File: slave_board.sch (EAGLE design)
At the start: 150 parts, among them IC3 ATMEGA2560-16AU, J11 1935161, J17 RJ45, J22 RJ45, J3 1935161, J6 1935161, K1 ORWH-SH-112D1F, Q1 PHB45NQ15T, Q2 PHB45NQ15T, Q3 BSS138L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

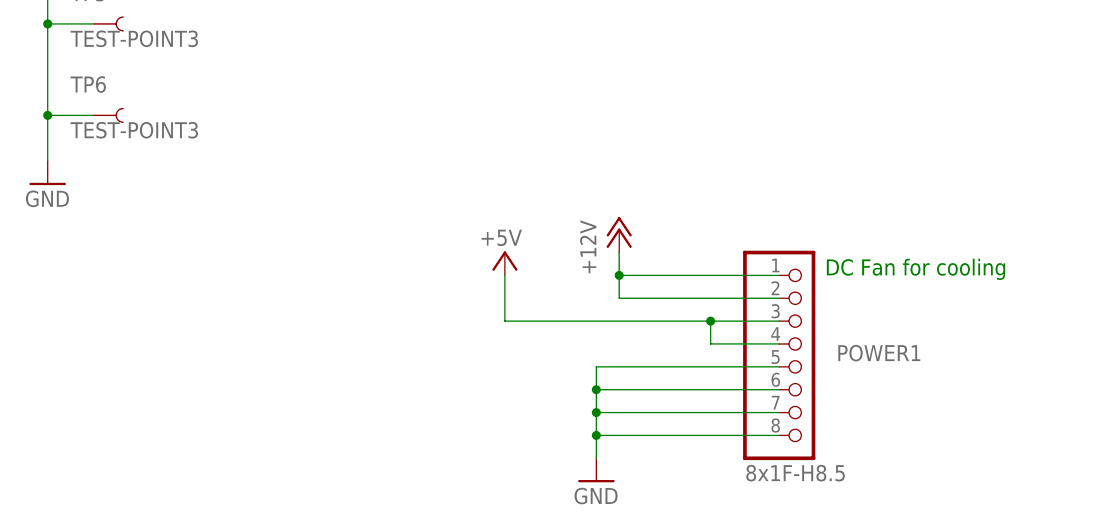
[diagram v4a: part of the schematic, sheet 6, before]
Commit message: More screw terminals
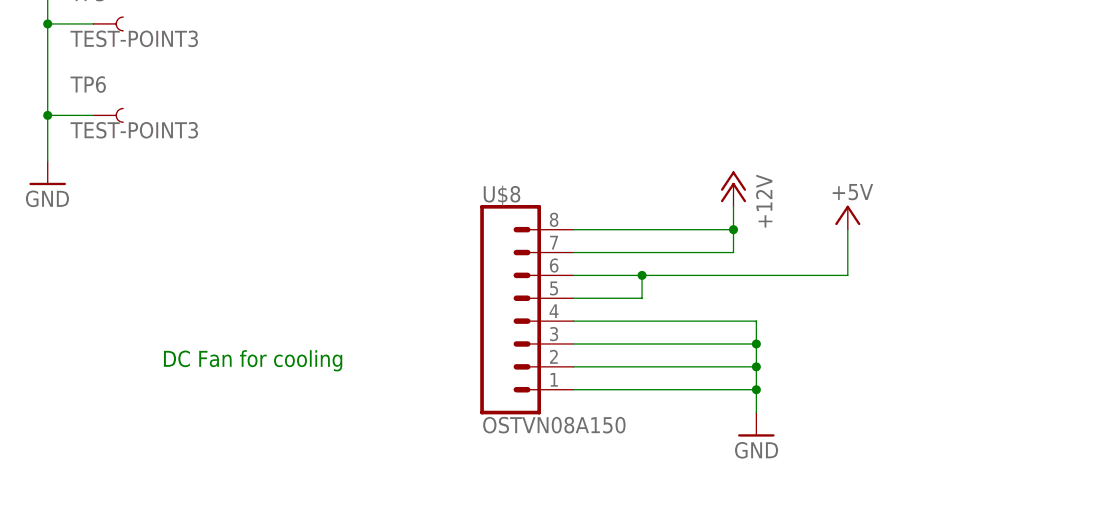
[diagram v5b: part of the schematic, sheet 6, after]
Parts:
- removed POWER1: 8x1F-H8.5, SmartPrj:PINHD-1X8
- added U$8: OSTVN08A150, smoothio:OSTVN08A150
- J18, J8: value (none) -> OSTVN08A150; device SparkFun-Connectors:CONN_08" -> smoothio:OSTVN08A150
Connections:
- net +12V: now also U$8.7, U$8.8; no longer POWER1.1, POWER1.2
- net +5V: now also U$8.5, U$8.6; no longer POWER1.3, POWER1.4
- net GND: now also U$8.1, U$8.2, U$8.3, U$8.4; no longer POWER1.5, POWER1.6, POWER1.7, POWER1.8
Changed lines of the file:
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@@
 <part name="GND83" library="supply1" library_urn="urn:adsk.eagle:library:371" deviceset="GND" device=""/>
 <part name="P+14" library="supply1" library_urn="urn:adsk.eagle:library:371" deviceset="+5V" device=""/>
-<part name="POWER1" library="SmartPrj" deviceset="PINHD-1X8" device="" value="8x1F-H8.5"/>
 <part name="P+37" library="supply1" library_urn="urn:adsk.eagle:library:371" deviceset="+12V" device=""/>
 <part name="P+4" library="supply1" library_urn="urn:adsk.eagle:library:371" deviceset="+5V" device=""/>
@@
 <part name="P+42" library="supply1" library_urn="urn:adsk.eagle:library:371" deviceset="+5V" device=""/>
 <part name="C24" library="rcl" library_urn="urn:adsk.eagle:library:334" deviceset="C-US" device="C0603" package3d_urn="urn:adsk.eagle:package:23616/2" value="0.1uF"/>
-<part name="J8" library="SparkFun-Connectors" library_urn="urn:adsk.eagle:library:513" deviceset="CONN_08" device="&quot;" package3d_urn="urn:adsk.eagle:package:38138/1"/>
-<part name="J18" library="SparkFun-Connectors" library_urn="urn:adsk.eagle:library:513" deviceset="CONN_08" device="&quot;" package3d_urn="urn:adsk.eagle:package:38138/1"/>
+<part name="J8" library="smoothio" deviceset="OSTVN08A150" device=""/>
+<part name="J18" library="smoothio" deviceset="OSTVN08A150" device=""/>
 <part name="JP14" library="SparkFun-Jumpers" library_urn="urn:adsk.eagle:library:528" deviceset="JUMPER-SMT_2_NC_TRACE" device="_NO-SILK" package3d_urn="urn:adsk.eagle:package:39286/1"/>
 <part name="J7" library="SparkFun-Connectors" library_urn="urn:adsk.eagle:library:513" deviceset="CONN_02" device="" package3d_urn="urn:adsk.eagle:package:38039/1"/>
@@
 <part name="GND63" library="supply1" library_urn="urn:adsk.eagle:library:371" deviceset="GND" device=""/>
 <part name="P+16" library="supply1" library_urn="urn:adsk.eagle:library:371" deviceset="+5V" device=""/>
+<part name="U$8" library="smoothio" deviceset="OSTVN08A150" device=""/>
 </parts>
 <sheets>
@@
 <text x="119.38" y="127" size="1.778" layer="91">add heat sink to diodes</text>
 <text x="30.48" y="119.38" size="1.778" layer="91">AC Mains Switch: RA81231121</text>
-<text x="353.06" y="60.96" size="1.778" layer="91">DC Fan for cooling</text>
+<text x="279.4" y="50.8" size="1.778" layer="91">DC Fan for cooling</text>
 <text x="15.24" y="223.52" size="1.778" layer="91">drive voltage = 10V
 Id = -8.8A continuous</text>
@@
 <attribute name="VALUE" x="193.04" y="203.4286" size="1.778" layer="96"/>
 </instance>
-<instance part="GND83" gate="1" x="327.66" y="38.1" smashed="yes">
-<attribute name="VALUE" x="325.12" y="35.56" size="1.778" layer="96"/>
+<instance part="GND83" gate="1" x="345.44" y="43.18" smashed="yes" rot="MR0">
+<attribute name="VALUE" x="347.98" y="40.64" size="1.778" layer="96" rot="MR0"/>
 </instance>
-<instance part="P+14" gate="1" x="317.5" y="63.5" smashed="yes">
-<attribute name="VALUE" x="319.405" y="66.04" size="1.778" layer="96" rot="R180"/>
+<instance part="P+14" gate="1" x="355.6" y="68.58" smashed="yes" rot="MR0">
+<attribute name="VALUE" x="353.695" y="71.12" size="1.778" layer="96" rot="MR180"/>
 </instance>
-<instance part="POWER1" gate="A" x="350.52" y="50.8" smashed="yes">
-<attribute name="NAME" x="354.33" y="51.435" size="1.778" layer="95"/>
-<attribute name="VALUE" x="344.17" y="38.1" size="1.778" layer="96"/>
-</instance>
-<instance part="P+37" gate="1" x="330.2" y="66.04" smashed="yes">
-<attribute name="VALUE" x="327.66" y="60.96" size="1.778" layer="96" rot="R90"/>
+<instance part="P+37" gate="1" x="342.9" y="71.12" smashed="yes" rot="MR0">
+<attribute name="VALUE" x="345.44" y="66.04" size="1.778" layer="96" rot="MR90"/>
 </instance>
 <instance part="U8" gate="G$1" x="226.06" y="205.74" smashed="yes">
@@
 <attribute name="VALUE" x="330.2" y="195.58" size="1.778" layer="96"/>
 </instance>
+<instance part="U$8" gate="G$1" x="320.04" y="55.88" smashed="yes">
+<attribute name="VALUE" x="314.96" y="43.434" size="1.778" layer="96" font="vector"/>
+<attribute name="NAME" x="314.96" y="69.088" size="1.778" layer="95" font="vector"/>
+</instance>
 </instances>
 <busses>
@@
 </segment>
 <segment>
-<pinref part="POWER1" gate="A" pin="1"/>
-<wire x1="347.98" y1="60.96" x2="330.2" y2="60.96" width="0.1524" layer="91"/>
-<wire x1="330.2" y1="60.96" x2="330.2" y2="63.5" width="0.1524" layer="91"/>
+<wire x1="325.12" y1="66.04" x2="342.9" y2="66.04" width="0.1524" layer="91"/>
+<wire x1="342.9" y1="66.04" x2="342.9" y2="68.58" width="0.1524" layer="91"/>
 <pinref part="P+37" gate="1" pin="+12V"/>
-<pinref part="POWER1" gate="A" pin="2"/>
-<wire x1="347.98" y1="58.42" x2="330.2" y2="58.42" width="0.1524" layer="91"/>
-<wire x1="330.2" y1="58.42" x2="330.2" y2="60.96" width="0.1524" layer="91"/>
-<junction x="330.2" y="60.96"/>
+<wire x1="325.12" y1="63.5" x2="342.9" y2="63.5" width="0.1524" layer="91"/>
+<wire x1="342.9" y1="63.5" x2="342.9" y2="66.04" width="0.1524" layer="91"/>
+<junction x="342.9" y="66.04"/>
+<pinref part="U$8" gate="G$1" pin="7"/>
+<pinref part="U$8" gate="G$1" pin="8"/>
 </segment>
 <segment>
@@
 </segment>
 <segment>
-<wire x1="347.98" y1="48.26" x2="327.66" y2="48.26" width="0.1524" layer="91"/>
-<wire x1="327.66" y1="48.26" x2="327.66" y2="45.72" width="0.1524" layer="91"/>
-<wire x1="347.98" y1="45.72" x2="327.66" y2="45.72" width="0.1524" layer="91"/>
-<wire x1="327.66" y1="45.72" x2="327.66" y2="43.18" width="0.1524" layer="91"/>
-<junction x="327.66" y="45.72"/>
+<wire x1="325.12" y1="53.34" x2="345.44" y2="53.34" width="0.1524" layer="91"/>
+<wire x1="345.44" y1="53.34" x2="345.44" y2="50.8" width="0.1524" layer="91"/>
+<wire x1="325.12" y1="50.8" x2="345.44" y2="50.8" width="0.1524" layer="91"/>
+<wire x1="345.44" y1="50.8" x2="345.44" y2="48.26" width="0.1524" layer="91"/>
+<junction x="345.44" y="50.8"/>
 <pinref part="GND83" gate="1" pin="GND"/>
-<pinref part="POWER1" gate="A" pin="6"/>
-<pinref part="POWER1" gate="A" pin="7"/>
-<pinref part="POWER1" gate="A" pin="8"/>
-<wire x1="327.66" y1="43.18" x2="327.66" y2="40.64" width="0.1524" layer="91"/>
-<wire x1="347.98" y1="43.18" x2="327.66" y2="43.18" width="0.1524" layer="91"/>
-<junction x="327.66" y="43.18"/>
-<pinref part="POWER1" gate="A" pin="5"/>
-<wire x1="347.98" y1="50.8" x2="327.66" y2="50.8" width="0.1524" layer="91"/>
-<wire x1="327.66" y1="50.8" x2="327.66" y2="48.26" width="0.1524" layer="91"/>
-<junction x="327.66" y="48.26"/>
+<wire x1="345.44" y1="48.26" x2="345.44" y2="45.72" width="0.1524" layer="91"/>
+<wire x1="325.12" y1="48.26" x2="345.44" y2="48.26" width="0.1524" layer="91"/>
+<junction x="345.44" y="48.26"/>
+<wire x1="325.12" y1="55.88" x2="345.44" y2="55.88" width="0.1524" layer="91"/>
+<wire x1="345.44" y1="55.88" x2="345.44" y2="53.34" width="0.1524" layer="91"/>
+<junction x="345.44" y="53.34"/>
+<pinref part="U$8" gate="G$1" pin="1"/>
+<pinref part="U$8" gate="G$1" pin="2"/>
+<pinref part="U$8" gate="G$1" pin="3"/>
+<pinref part="U$8" gate="G$1" pin="4"/>
 </segment>
 <segment>
@@
 <segment>
 <pinref part="P+14" gate="1" pin="+5V"/>
-<wire x1="317.5" y1="60.96" x2="317.5" y2="55.88" width="0.1524" layer="91"/>
-<pinref part="POWER1" gate="A" pin="3"/>
-<wire x1="317.5" y1="55.88" x2="340.36" y2="55.88" width="0.1524" layer="91"/>
-<pinref part="POWER1" gate="A" pin="4"/>
-<wire x1="340.36" y1="55.88" x2="347.98" y2="55.88" width="0.1524" layer="91"/>
-<wire x1="347.98" y1="53.34" x2="340.36" y2="53.34" width="0.1524" layer="91"/>
-<wire x1="340.36" y1="53.34" x2="340.36" y2="55.88" width="0.1524" layer="91"/>
-<junction x="340.36" y="55.88"/>
+<wire x1="355.6" y1="66.04" x2="355.6" y2="60.96" width="0.1524" layer="91"/>
+<wire x1="355.6" y1="60.96" x2="332.74" y2="60.96" width="0.1524" layer="91"/>
+<wire x1="332.74" y1="60.96" x2="325.12" y2="60.96" width="0.1524" layer="91"/>
+<wire x1="325.12" y1="58.42" x2="332.74" y2="58.42" width="0.1524" layer="91"/>
+<wire x1="332.74" y1="58.42" x2="332.74" y2="60.96" width="0.1524" layer="91"/>
+<junction x="332.74" y="60.96"/>
+<pinref part="U$8" gate="G$1" pin="5"/>
+<pinref part="U$8" gate="G$1" pin="6"/>
 </segment>
 </net>

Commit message: board progress
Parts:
- added H1, H2, H3, H4: MOUNT-HOLE3.3, holes:MOUNT-HOLE3.3
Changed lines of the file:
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@@
 <part name="P+16" library="supply1" library_urn="urn:adsk.eagle:library:371" deviceset="+5V" device=""/>
 <part name="U$8" library="smoothio" deviceset="OSTVN08A150" device=""/>
+<part name="H1" library="holes" library_urn="urn:adsk.eagle:library:237" deviceset="MOUNT-HOLE" device="3.3" package3d_urn="urn:adsk.eagle:package:14278/1"/>
+<part name="H2" library="holes" library_urn="urn:adsk.eagle:library:237" deviceset="MOUNT-HOLE" device="3.3" package3d_urn="urn:adsk.eagle:package:14278/1"/>
+<part name="H3" library="holes" library_urn="urn:adsk.eagle:library:237" deviceset="MOUNT-HOLE" device="3.3" package3d_urn="urn:adsk.eagle:package:14278/1"/>
+<part name="H4" library="holes" library_urn="urn:adsk.eagle:library:237" deviceset="MOUNT-HOLE" device="3.3" package3d_urn="urn:adsk.eagle:package:14278/1"/>
+<part name="GND64" library="supply1" library_urn="urn:adsk.eagle:library:371" deviceset="GND" device=""/>
 </parts>
 <sheets>
@@
 <attribute name="NAME" x="74.676" y="160.401" size="1.778" layer="95" rot="MR0"/>
 <attribute name="VALUE" x="74.676" y="155.321" size="1.778" layer="96" rot="MR0"/>
+</instance>
+<instance part="H1" gate="G$1" x="142.24" y="228.6" smashed="yes">
+<attribute name="NAME" x="144.272" y="229.1842" size="1.778" layer="95"/>
+<attribute name="VALUE" x="144.272" y="226.1362" size="1.778" layer="96"/>
+</instance>
+<instance part="H2" gate="G$1" x="142.24" y="223.52" smashed="yes">
+<attribute name="NAME" x="144.272" y="224.1042" size="1.778" layer="95"/>
+<attribute name="VALUE" x="144.272" y="221.0562" size="1.778" layer="96"/>
+</instance>
+<instance part="H3" gate="G$1" x="142.24" y="218.44" smashed="yes">
+<attribute name="NAME" x="144.272" y="219.0242" size="1.778" layer="95"/>
+<attribute name="VALUE" x="144.272" y="215.9762" size="1.778" layer="96"/>
+</instance>
+<instance part="H4" gate="G$1" x="142.24" y="213.36" smashed="yes">
+<attribute name="NAME" x="144.272" y="213.9442" size="1.778" layer="95"/>
+<attribute name="VALUE" x="144.272" y="210.8962" size="1.778" layer="96"/>
+</instance>
+<instance part="GND64" gate="1" x="129.54" y="203.2" smashed="yes">
+<attribute name="VALUE" x="127" y="200.66" size="1.778" layer="96"/>
 </instance>
 </instances>
@@
 <pinref part="GND82" gate="1" pin="GND"/>
 </segment>
+<segment>
+<pinref part="GND64" gate="1" pin="GND"/>
+<wire x1="142.24" y1="228.6" x2="129.54" y2="228.6" width="0.1524" layer="91"/>
+<wire x1="129.54" y1="228.6" x2="129.54" y2="223.52" width="0.1524" layer="91"/>
+<wire x1="129.54" y1="223.52" x2="129.54" y2="218.44" width="0.1524" layer="91"/>
+<wire x1="129.54" y1="218.44" x2="129.54" y2="213.36" width="0.1524" layer="91"/>
+<wire x1="129.54" y1="213.36" x2="129.54" y2="205.74" width="0.1524" layer="91"/>
+<wire x1="142.24" y1="223.52" x2="129.54" y2="223.52" width="0.1524" layer="91"/>
+<junction x="129.54" y="223.52"/>
+<wire x1="142.24" y1="218.44" x2="129.54" y2="218.44" width="0.1524" layer="91"/>
+<junction x="129.54" y="218.44"/>
+<wire x1="142.24" y1="213.36" x2="129.54" y2="213.36" width="0.1524" layer="91"/>
+<junction x="129.54" y="213.36"/>
+</segment>
 </net>
